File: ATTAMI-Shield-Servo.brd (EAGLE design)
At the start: 22.8 x 22.9 mm, 24 parts, among them U1 MIC5225, U2 ATTINY85

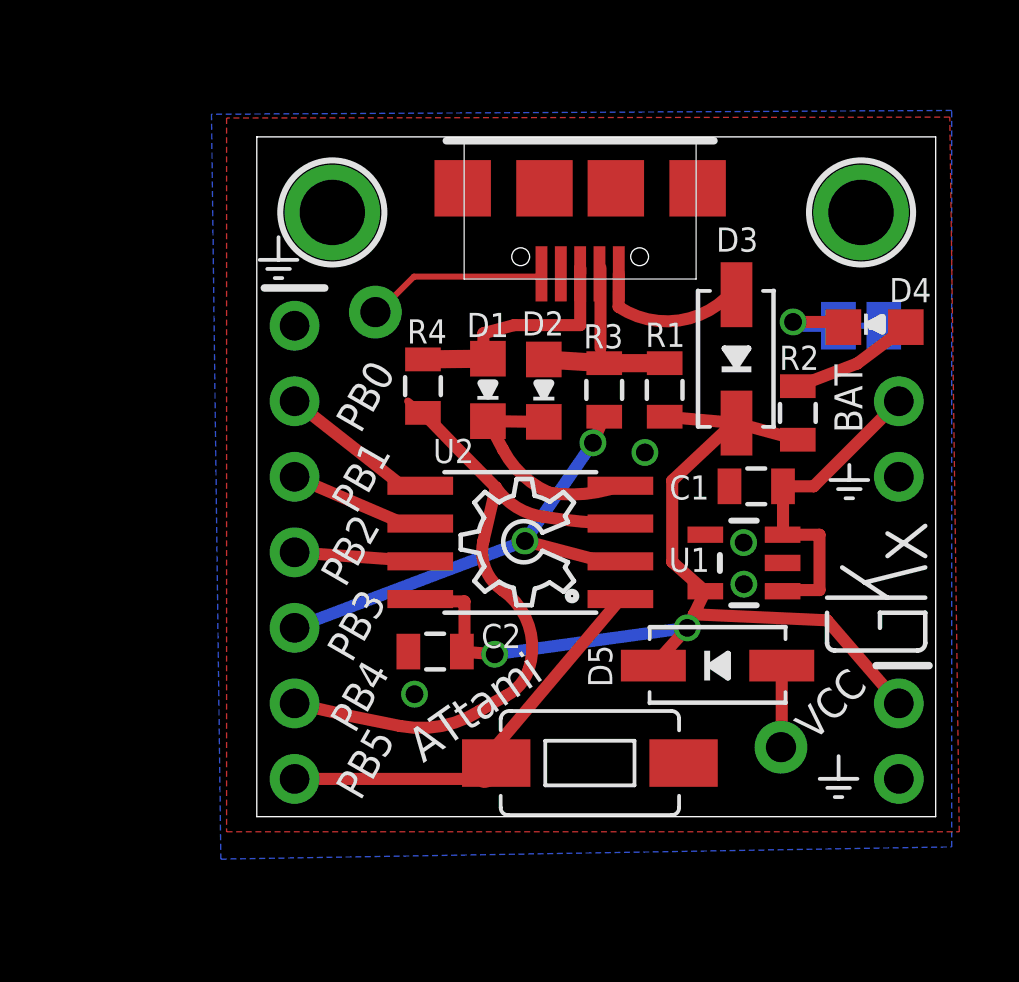
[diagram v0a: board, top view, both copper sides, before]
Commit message: servo shield - new
also added names and labels on wires
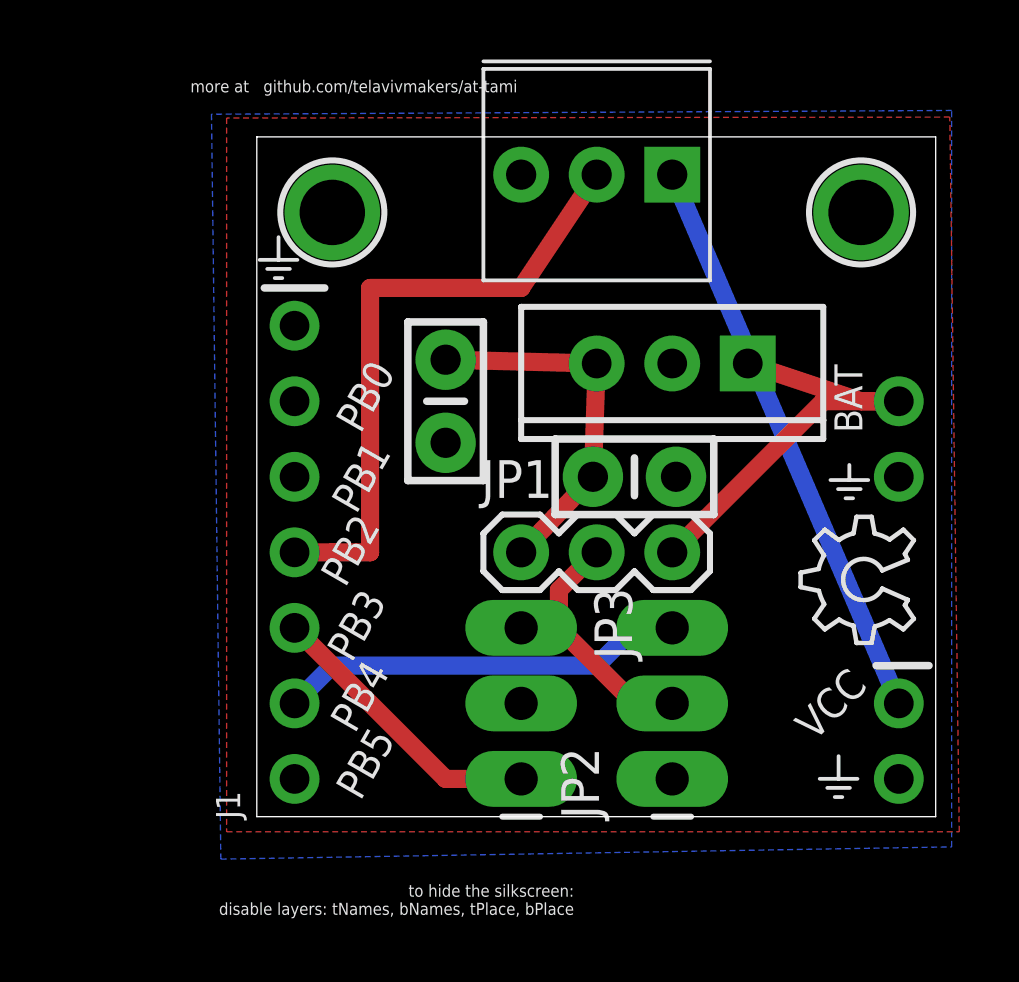
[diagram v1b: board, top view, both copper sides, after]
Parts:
- removed COIN_CELL_(+), COIN_CELL_(-): (no value), adafruit:1X01-CLEANBIG
- removed D1, D2: Blue LED, dp_devices:LED-805
- removed D3, D5: Schottky, microbuilder:SOD-323
- removed D4: Red LED, dp_devices:LED-805
- removed R1, R2: 1K5, SparkFun:0805
- removed R3, R4: 68R, SparkFun:0805
- removed S1: SWITCH-MOMENTARY-2-SMD-1101NE, SparkFun-Electromechanical:TACTILE-SWITCH-1101NE
- removed SJ1: (no value), microbuilder:SOLDERJUMPER_CLOSEDWIRE
- removed U1: MIC5225, SparkFun:SOT23-5
- removed U2: ATTINY85, SparkFun:SO08-EIAJ
- removed USB: MICRO-USB_ALIEXPRESS, yair_r:USB-MICRO-ALIEXPRESS
- added IC1: (no value), SparkFun-PowerIC:TO220-IGO
- added JP1: JUMPER-3PTH, SparkFun-Passives:1X03
- added JP2: servo1, SparkFun-Connectors:1X03_LONGPADS
- added JP3: servo2, SparkFun-Connectors:1X03_LONGPADS
- added POT: (no value), SparkFun-Electromechanical:3362U
- C1: value 1uf/25V -> (none); device SparkFun:0805 -> SparkFun-Capacitors:CAP-PTH-SMALL-KIT
- C2: value 2.2uf/16V -> (none); device SparkFun:0805 -> SparkFun-Capacitors:CAP-PTH-SMALL-KIT
- moved U$3 11.5 mm to (22.1, 5.84)
- moved C2 8.42 mm to (6.35, 14.0), turned to 270 degrees
- moved C1 4.11 mm to (12.7, 11.4), turned to 0 degrees
- turned J1 to 90 degrees
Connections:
- removed net N$10: D2.A, R1.2, R3.1, USB.DM
- removed net N$11: D4.A, R2.1
- removed net N$13: D4.C, SJ1.2
- removed net N$4: COIN_CELL_(+).1, D5.AQ
- removed net N$7: D1.A, R4.1, USB.DP
- removed net PB0: J1.2, U2.5
- removed net PB1: J1.3, U2.6
- removed net PB2: J1.4, U2.7
- removed net PB3: J1.5, R3.2, U2.2
- removed net PB4: J1.6, R4.2, U2.3
- removed net PB5: J1.7, S1.P$2, U2.1
- removed net V-BUS: D3.AQ, USB.VCC
- new net PB0(MOSI,PWM): J1.2, JP2.3
- new net PB1(MISO,PWM): J1.3, JP3.3
- new net PB2(ADC1\SCK): J1.4, POT.P$2
- new net PB3(ADC3): J1.5
- new net PB4(ADC2): J1.6
- new net PB5(RESET): J1.7
- new net VM: JP1.2, JP2.2, JP3.1
- new net V_REG: C1.1, C2.1, IC1.OUT, JP1.1
- net GND: now also IC1.GND, JP2.1, JP3.2, POT.P$3; no longer COIN_CELL_(-).1, D1.C, D2.C, S1.P$1, SJ1.1, U1.2, U2.4, USB.GND@1
- net VCC: now also POT.P$1; no longer C2.1, D3.CQ, D5.CQ, R1.1, R2.2, U1.5, U2.8
- net V_BAT: now also IC1.IN, JP1.3; no longer C1.1, U1.1, U1.3
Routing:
- net PB4: track 23.6 -> 0.00 mm
- net PB2(ADC1\SCK): track 0.00 -> 21.1 mm
- net PB3: track 16.5 -> 0.00 mm, vias 2 -> 0
- net VCC: track 35.2 -> 19.3 mm, vias 2 -> 0
- net PB5: track 15.0 -> 0.00 mm
- net PB0(MOSI,PWM): track 0.00 -> 13.8 mm
- net GND: track 13.6 -> 0.00 mm, vias 4 -> 0
- net V_REG: track 0.00 -> 12.5 mm
- net PB1(MISO,PWM): track 0.00 -> 9.72 mm
- net VM: track 0.00 -> 9.20 mm
- net N$7: track 8.52 -> 0.00 mm
- net N$10: track 7.49 -> 0.00 mm
- net PB0: track 5.19 -> 0.00 mm
- net V-BUS: track 5.19 -> 0.00 mm
- net PB1: track 4.54 -> 0.00 mm
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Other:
- board text added: "more at github.com/telavivmakers/at-tami"
- board text added: "to hide the silkscreen: disable layers: tNames, bNames, tPlace, bPlace"
- board text removed: "ATtami"

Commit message: flipped servo power pins
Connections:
- removed net VM: JP1.2, JP2.2, JP3.1
- new net V_IN: IC1.IN
- new net V_SERVO: JP1.2, JP3.2
- net GND: now also JP2.2; no longer JP2.1, JP3.2
- net V_BAT: no longer IC1.IN
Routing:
- net VM: track 9.20 -> 0.00 mm
- net V_SERVO: track 0.00 -> 6.66 mm
- net V_BAT: track 15.0 -> 11.0 mm
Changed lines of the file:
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@@
 <contactref element="J2" pad="2"/>
 <contactref element="J1" pad="1"/>
-<contactref element="JP2" pad="1"/>
-<contactref element="JP3" pad="2"/>
 <contactref element="POT" pad="P$3"/>
 <contactref element="IC1" pad="GND"/>
 <contactref element="C1" pad="2"/>
 <contactref element="C2" pad="2"/>
+<contactref element="JP2" pad="2"/>
+<wire x1="14.097" y1="11.43" x2="21.59" y2="11.43" width="0" layer="19" extent="1-1"/>
+<wire x1="13.97" y1="15.24" x2="14.097" y2="11.43" width="0" layer="19" extent="1-1"/>
+<wire x1="13.97" y1="3.81" x2="14.097" y2="11.43" width="0" layer="19" extent="1-1"/>
+<wire x1="6.35" y1="12.573" x2="14.097" y2="11.43" width="0" layer="19" extent="1-1"/>
+<wire x1="21.59" y1="1.27" x2="13.97" y2="3.81" width="0" layer="19" extent="1-1"/>
+<wire x1="8.89" y1="21.59" x2="13.97" y2="15.24" width="0" layer="19" extent="1-1"/>
+<wire x1="1.27" y1="1.27" x2="6.35" y2="12.573" width="0" layer="19" extent="1-1"/>
 </signal>
 <signal name="VCC">
@@
 <signal name="V_BAT">
 <contactref element="J2" pad="1"/>
-<contactref element="IC1" pad="IN"/>
 <contactref element="JP1" pad="3"/>
-<wire x1="16.51" y1="15.24" x2="20.32" y2="13.97" width="0.6096" layer="1"/>
 <wire x1="20.32" y1="13.97" x2="21.59" y2="13.97" width="0.6096" layer="1"/>
 <wire x1="21.59" y1="13.97" x2="19.05" y2="13.97" width="0.6096" layer="1"/>
@@
 <contactref element="J1" pad="7"/>
 </signal>
-<signal name="VM">
+<signal name="V_SERVO">
 <contactref element="JP1" pad="2"/>
-<contactref element="JP2" pad="2"/>
-<contactref element="JP3" pad="1"/>
-<wire x1="13.97" y1="3.81" x2="12.7" y2="3.81" width="0.6096" layer="1"/>
 <wire x1="12.7" y1="3.81" x2="10.16" y2="6.35" width="0.6096" layer="1"/>
-<wire x1="10.16" y1="6.35" x2="8.89" y2="6.35" width="0.6096" layer="1"/>
 <wire x1="10.16" y1="6.35" x2="10.16" y2="7.62" width="0.6096" layer="1"/>
 <wire x1="10.16" y1="7.62" x2="11.43" y2="8.89" width="0.6096" layer="1"/>
+<contactref element="JP3" pad="2"/>
+<wire x1="8.89" y1="3.81" x2="10.16" y2="6.35" width="0" layer="19" extent="1-1"/>
 </signal>
 <signal name="V_REG">
@@
 <wire x1="11.303" y1="11.43" x2="8.89" y2="8.89" width="0.6096" layer="1"/>
 </signal>
+<signal name="V_IN">
+<contactref element="IC1" pad="IN"/>
+</signal>
 </signals>

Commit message: servo shield
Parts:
- added J4: (no value), microbuilder:1X02_ROUND
- JP1: value JUMPER-3PTH -> JUMPER-power
- moved J3 2.84 mm to (20.3, 5.08)
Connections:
- removed net V_REG: C1.1, C2.1, IC1.OUT, JP1.1
- removed net V_SERVO: JP1.2, JP3.2
- new net N$3: IC1.OUT, JP1.1
- net GND: now also J4.2, JP2.1, JP3.1; no longer JP2.2
- net VCC: no longer J3.1
- net V_BAT: now also C1.1, C2.1, JP1.2, JP2.2, JP3.2; no longer JP1.3
- net V_IN: now also J3.1, J4.1, JP1.3
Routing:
- net VCC: track 19.3 -> 0.00 mm
- net V_REG: track 12.5 -> 0.00 mm
- net V_BAT: track 11.0 -> 3.81 mm
- net V_SERVO: track 6.66 -> 0.00 mm
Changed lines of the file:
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@@
 <setting verticaltext="up"/>
 </settings>
-<grid distance="100" unitdist="mil" unit="mil" style="lines" multiple="1" display="yes" altdistance="50" altunitdist="mil" altunit="mil"/>
+<grid distance="50" unitdist="mil" unit="mil" style="lines" multiple="1" display="yes" altdistance="10" altunitdist="mil" altunit="mil"/>
 <layers>
 <layer number="1" name="Top" color="4" fill="1" visible="yes" active="yes"/>
@@
 <layer number="21" name="tPlace" color="7" fill="1" visible="no" active="yes"/>
 <layer number="22" name="bPlace" color="7" fill="1" visible="no" active="yes"/>
-<layer number="23" name="tOrigins" color="15" fill="1" visible="no" active="yes"/>
+<layer number="23" name="tOrigins" color="15" fill="1" visible="yes" active="yes"/>
 <layer number="24" name="bOrigins" color="15" fill="1" visible="no" active="yes"/>
 <layer number="25" name="tNames" color="7" fill="1" visible="no" active="yes"/>
@@
 <attribute name="NAME" x="20.843240625" y="8.666478125" size="1.27" layer="37" ratio="10"/>
 </element>
-<element name="J3" library="microbuilder" package="1X02_ROUND" value="" x="21.59" y="2.54" smashed="yes" rot="R270">
-<attribute name="NAME" x="20.77211875" y="5.6286375" size="1.27" layer="37" ratio="10"/>
-</element>
 <element name="U$3" library="ohw-logo" package="OSHW_6X150_NOTEXT" value="" x="22.098" y="5.842" rot="R90"/>
 <element name="JP2" library="SparkFun-Connectors" package="1X03_LONGPADS" value="servo1" x="13.97" y="1.27" rot="R90"/>
@@
 <element name="J1" library="microbuilder" package="1X07_ROUND" value="" x="1.27" y="8.89" rot="R90"/>
 <element name="C2" library="SparkFun-Capacitors" package="CAP-PTH-SMALL-KIT" value="" x="6.35" y="13.97" rot="R270"/>
-<element name="JP1" library="SparkFun-Passives" package="1X03" value="JUMPER-3PTH" x="8.89" y="8.89"/>
+<element name="JP1" library="SparkFun-Passives" package="1X03" value="JUMPER-power" x="8.89" y="8.89"/>
+<element name="J3" library="microbuilder" package="1X02_ROUND" value="" x="20.32" y="5.08" rot="R270"/>
+<element name="J4" library="microbuilder" package="1X02_ROUND" value="" x="0" y="-7.62"/>
 </elements>
 <signals>
 <signal name="GND">
-<contactref element="J3" pad="2"/>
 <polygon width="0.4064" layer="16" isolate="0.3302">
 <vertex x="23.368" y="23.749"/>
@@
 <contactref element="J1" pad="1"/>
 <contactref element="POT" pad="P$3"/>
+<contactref element="JP3" pad="1"/>
+<contactref element="J3" pad="2"/>
+<contactref element="JP2" pad="1"/>
 <contactref element="IC1" pad="GND"/>
 <contactref element="C1" pad="2"/>
 <contactref element="C2" pad="2"/>
-<contactref element="JP2" pad="2"/>
+<contactref element="J4" pad="2"/>
 <wire x1="14.097" y1="11.43" x2="21.59" y2="11.43" width="0" layer="19" extent="1-1"/>
 <wire x1="13.97" y1="15.24" x2="14.097" y2="11.43" width="0" layer="19" extent="1-1"/>
-<wire x1="13.97" y1="3.81" x2="14.097" y2="11.43" width="0" layer="19" extent="1-1"/>
-<wire x1="6.35" y1="12.573" x2="14.097" y2="11.43" width="0" layer="19" extent="1-1"/>
-<wire x1="21.59" y1="1.27" x2="13.97" y2="3.81" width="0" layer="19" extent="1-1"/>
+<wire x1="8.89" y1="6.35" x2="14.097" y2="11.43" width="0" layer="19" extent="1-1"/>
+<wire x1="6.35" y1="12.573" x2="8.89" y2="6.35" width="0" layer="19" extent="1-1"/>
+<wire x1="13.97" y1="1.27" x2="8.89" y2="6.35" width="0" layer="19" extent="1-1"/>
+<wire x1="20.32" y1="3.81" x2="13.97" y2="1.27" width="0" layer="19" extent="1-1"/>
 <wire x1="8.89" y1="21.59" x2="13.97" y2="15.24" width="0" layer="19" extent="1-1"/>
-<wire x1="1.27" y1="1.27" x2="6.35" y2="12.573" width="0" layer="19" extent="1-1"/>
+<wire x1="1.27" y1="1.27" x2="8.89" y2="6.35" width="0" layer="19" extent="1-1"/>
+<wire x1="1.27" y1="-7.62" x2="1.27" y2="1.27" width="0" layer="19" extent="1-1"/>
 </signal>
 <signal name="VCC">
-<contactref element="J3" pad="1"/>
 <contactref element="POT" pad="P$1"/>
-<wire x1="21.59" y1="3.81" x2="13.97" y2="21.59" width="0.6096" layer="16"/>
 </signal>
 <signal name="N$2">
@@
 <signal name="V_BAT">
 <contactref element="J2" pad="1"/>
-<contactref element="JP1" pad="3"/>
 <wire x1="20.32" y1="13.97" x2="21.59" y2="13.97" width="0.6096" layer="1"/>
 <wire x1="21.59" y1="13.97" x2="19.05" y2="13.97" width="0.6096" layer="1"/>
-<wire x1="19.05" y1="13.97" x2="13.97" y2="8.89" width="0.6096" layer="1"/>
+<contactref element="JP1" pad="2"/>
+<contactref element="JP3" pad="2"/>
+<contactref element="JP2" pad="2"/>
+<contactref element="C1" pad="1"/>
+<contactref element="C2" pad="1"/>
+<wire x1="11.303" y1="11.43" x2="19.05" y2="13.97" width="0" layer="19" extent="1-1"/>
+<wire x1="11.43" y1="8.89" x2="11.303" y2="11.43" width="0" layer="19" extent="1-1"/>
+<wire x1="13.97" y1="3.81" x2="11.43" y2="8.89" width="0" layer="19" extent="1-1"/>
+<wire x1="8.89" y1="3.81" x2="13.97" y2="3.81" width="0" layer="19" extent="1-1"/>
+<wire x1="6.35" y1="15.367" x2="11.303" y2="11.43" width="0" layer="19" extent="1-1"/>
 </signal>
 <signal name="PB0(MOSI,PWM)">
@@
 <contactref element="J1" pad="7"/>
 </signal>
-<signal name="V_SERVO">
-<contactref element="JP1" pad="2"/>
-<wire x1="12.7" y1="3.81" x2="10.16" y2="6.35" width="0.6096" layer="1"/>
-<wire x1="10.16" y1="6.35" x2="10.16" y2="7.62" width="0.6096" layer="1"/>
-<wire x1="10.16" y1="7.62" x2="11.43" y2="8.89" width="0.6096" layer="1"/>
-<contactref element="JP3" pad="2"/>
-<wire x1="8.89" y1="3.81" x2="10.16" y2="6.35" width="0" layer="19" extent="1-1"/>
-</signal>
-<signal name="V_REG">
+<signal name="V_IN">
+<contactref element="JP1" pad="3"/>
+<contactref element="J3" pad="1"/>
+<contactref element="J4" pad="1"/>
+<contactref element="IC1" pad="IN"/>
+<wire x1="13.97" y1="8.89" x2="16.51" y2="15.24" width="0" layer="19" extent="1-1"/>
+<wire x1="20.32" y1="6.35" x2="13.97" y2="8.89" width="0" layer="19" extent="1-1"/>
+<wire x1="-1.27" y1="-7.62" x2="13.97" y2="8.89" width="0" layer="19" extent="1-1"/>
+</signal>
+<signal name="N$3">
+<contactref element="IC1" pad="OUT"/>
 <contactref element="JP1" pad="1"/>
-<contactref element="IC1" pad="OUT"/>
-<contactref element="C1" pad="1"/>
-<contactref element="C2" pad="1"/>
-<wire x1="11.43" y1="15.367" x2="11.43" y2="15.24" width="0.6096" layer="1"/>
-<wire x1="6.35" y1="15.367" x2="11.43" y2="15.24" width="0.6096" layer="1"/>
-<wire x1="11.43" y1="15.24" x2="11.303" y2="11.43" width="0.6096" layer="1"/>
-<wire x1="11.303" y1="11.43" x2="8.89" y2="8.89" width="0.6096" layer="1"/>
-</signal>
-<signal name="V_IN">
-<contactref element="IC1" pad="IN"/>
+<wire x1="8.89" y1="8.89" x2="11.43" y2="15.24" width="0" layer="19" extent="1-1"/>
 </signal>
 </signals>

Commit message: servi inverter
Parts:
- added IC2: 7404D, 74xx-us:SO14
- added J5: (no value), microbuilder:1X02_ROUND
- added JP4: servo1_mirror, SparkFun-Connectors:1X03_LONGPADS
- added JP5: servo2_mirror, SparkFun-Connectors:1X03_LONGPADS
- added S1: SWITCH-MOMENTARY-2-SMD-1101NE, SparkFun-Electromechanical:TACTILE-SWITCH-1101NE
- added U$4, U$5: MOUNTINGHOLE2.0, microbuilder:MOUNTINGHOLE_2.0_PLATED
- moved J4 43.2 mm to (17.8, 31.8), turned to 270 degrees
- moved C1 19.1 mm to (11.4, 30.5)
- moved POT 19.0 mm to (14.0, 5.08)
- moved IC1 18.0 mm to (11.4, 33.0)
- moved J3 18.0 mm to (17.8, 22.9)
- moved JP1 17.8 mm to (8.89, 26.7)
- moved J2 15.2 mm to (21.6, 27.9)
- moved U$1 15.2 mm to (2.54, 35.6)
- moved U$2 15.2 mm to (20.3, 35.6)
- moved U$3 15.2 mm to (22.1, 21.1)
- moved J1 15.2 mm to (1.27, 24.1)
- moved C2 14.0 mm to (5.08, 27.9)
- moved JP2 8.98 mm to (20.3, 7.62), turned to 180 degrees
- moved JP3 6.48 mm to (2.54, 7.62), turned to 0 degrees
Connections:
- new net N$1: IC2.2, JP4.3
- new net N$5: IC2.4, JP5.3
- net GND: now also IC2.11, IC2.13, IC2.5, IC2.7, IC2.9, J5.2, JP4.1, JP5.1, S1.P$1
- net PB0(MOSI,PWM): now also IC2.1
- net PB1(MISO,PWM): now also IC2.3
- net PB5(RESET): now also S1.P$2
- net VCC: now also IC2.14, J5.1
- net V_BAT: now also JP4.2, JP5.2
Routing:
- net PB2(ADC1\SCK): track 21.1 -> 0.00 mm
- net PB0(MOSI,PWM): track 13.8 -> 0.00 mm
- net PB1(MISO,PWM): track 9.72 -> 0.00 mm
- net V_BAT: track 3.81 -> 0.00 mm
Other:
- board size 22.8 x 22.9 mm -> 22.8 x 38.1 mm

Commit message: servo shield-no invert :(
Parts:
- removed IC2: 7404D, 74xx-us:SO14
- moved JP2 8.24 mm to (17.9, 15.5)
- moved U$3 6.49 mm to (15.6, 21.5)
- moved JP5 5.24 mm to (4.57, 15.5)
- moved U$4 5.09 mm to (2.29, 7.62)
- moved U$5 4.83 mm to (20.2, 7.37)
- moved JP1 4.16 mm to (13.0, 27.6)
- moved JP3 4.11 mm to (3.17, 11.7)
- moved C1 3.81 mm to (9.53, 27.2), turned to 90 degrees
- moved J4 1.27 mm to (19.1, 31.8), turned to 0 degrees
- moved C2 1.17 mm to (5.97, 27.2), turned to 90 degrees
- moved J3 0.38 mm to (18.2, 22.9)
- turned J1 to 270 degrees
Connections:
- removed net N$1: IC2.2, JP4.3
- removed net N$5: IC2.4, JP5.3
- net GND: no longer IC2.11, IC2.13, IC2.5, IC2.7, IC2.9
- net PB0(MOSI,PWM): now also JP4.3; no longer IC2.1
- net PB1(MISO,PWM): now also JP5.3; no longer IC2.3
- net VCC: no longer IC2.14
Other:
- board text removed: "to hide the silkscreen: disable layers: tNames, bNames, tPlace, bPlace"
